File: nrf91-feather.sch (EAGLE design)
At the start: 90 parts, among them J1 CON-USB-1050170001, J2 CON-HEADER-1X12-MALE-PIN, J3 CON-HEADER-1X16-MALE-PIN, J4 CON-1909763-1, J5 CON-SIM-104224-0820, J6 CON-S2B-PH-SM4-TB(LF)(SN), J7 CON-1909763-1, J9 CON-TC2030-MCP-NL, Q1 MOSFET-P-SC89, Q2 MOSFET-DUAL-COMP-SOT563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

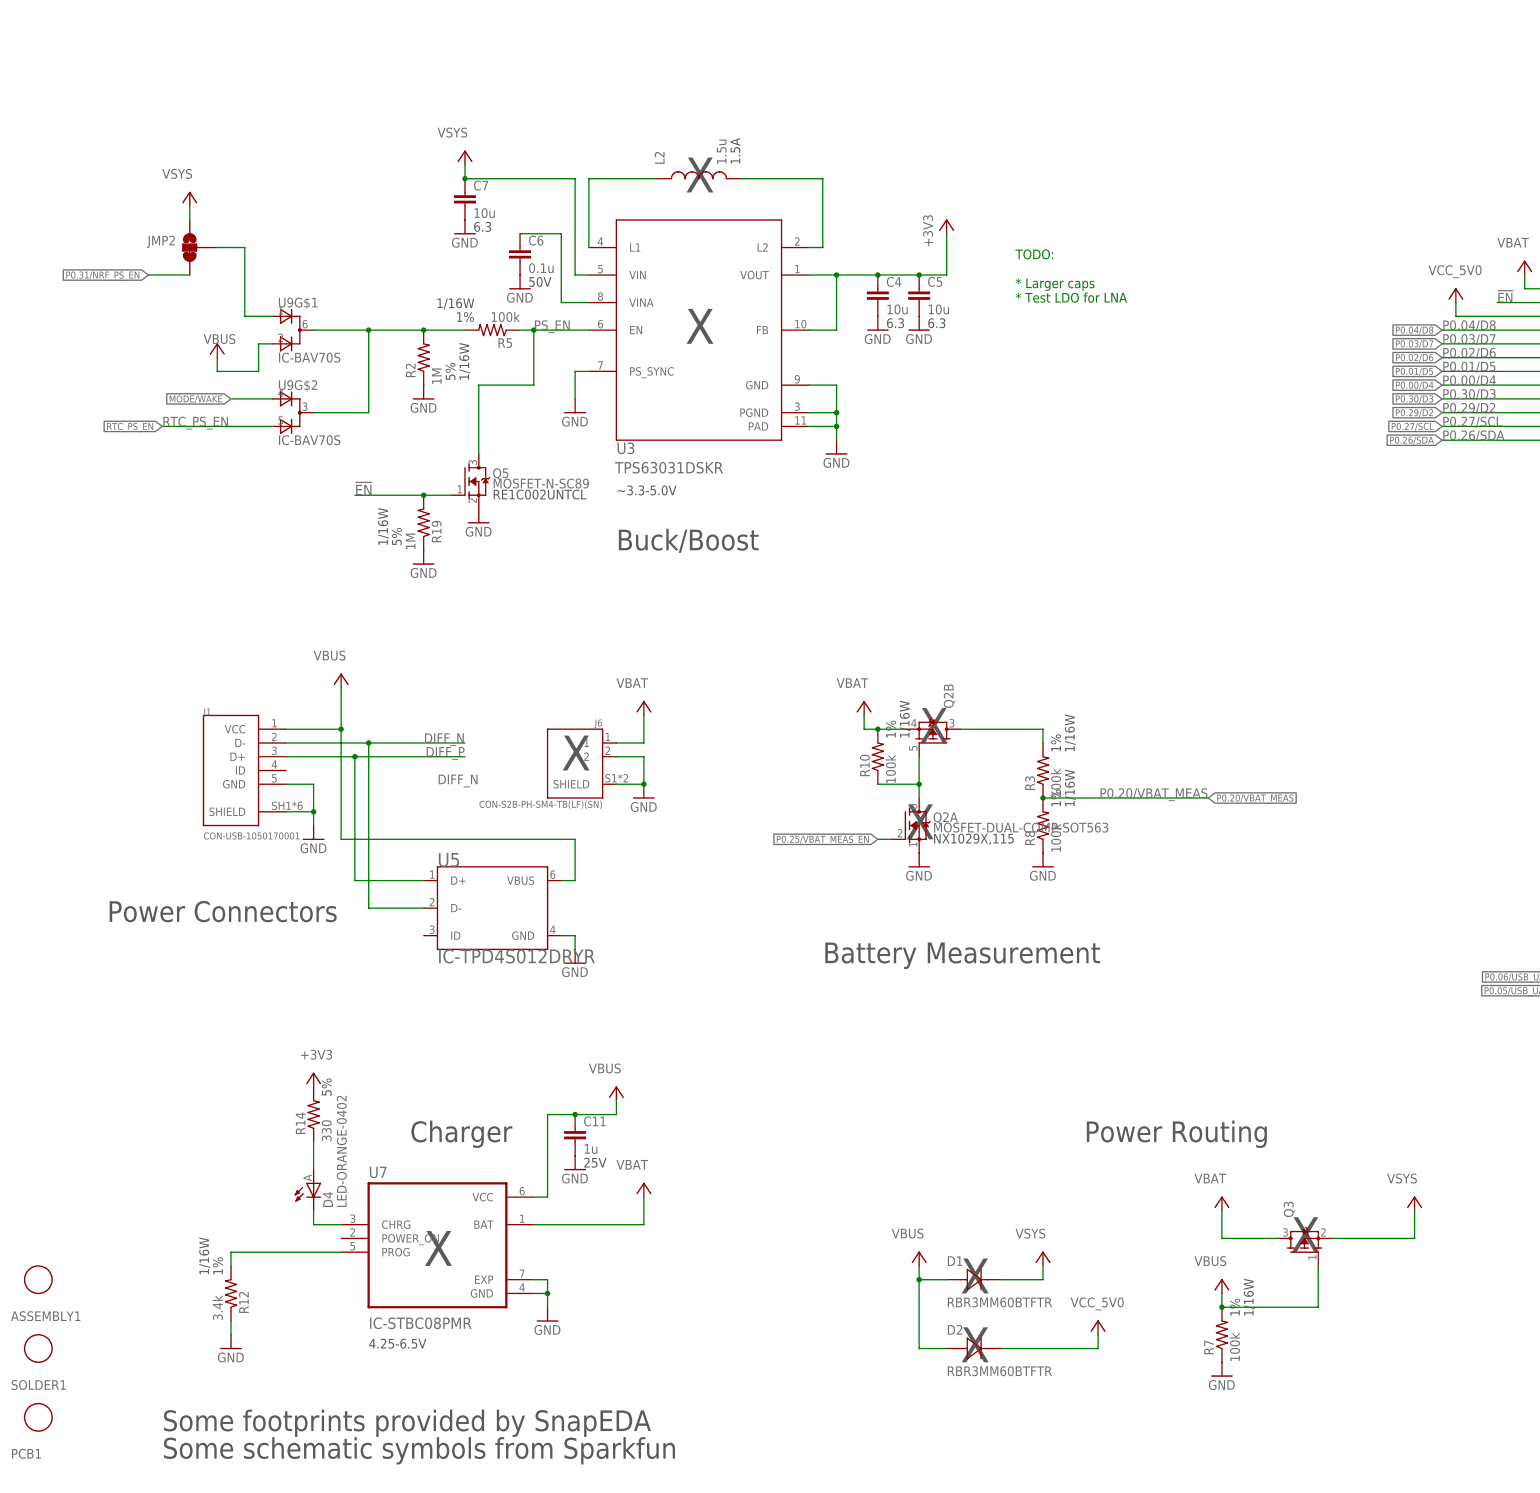
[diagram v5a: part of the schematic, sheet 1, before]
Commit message: Changes for next revision of the nRF9160 Feather
Removed:
* TVS diode

Changed:
* USB is now USB-C
* Power supply is now Boost + LDO combo (not final)
* LED position due to USB-C being larger
* Changed Schottky diodes to a TSC part
* Re-routed and cleaned up some signals on the inner layer
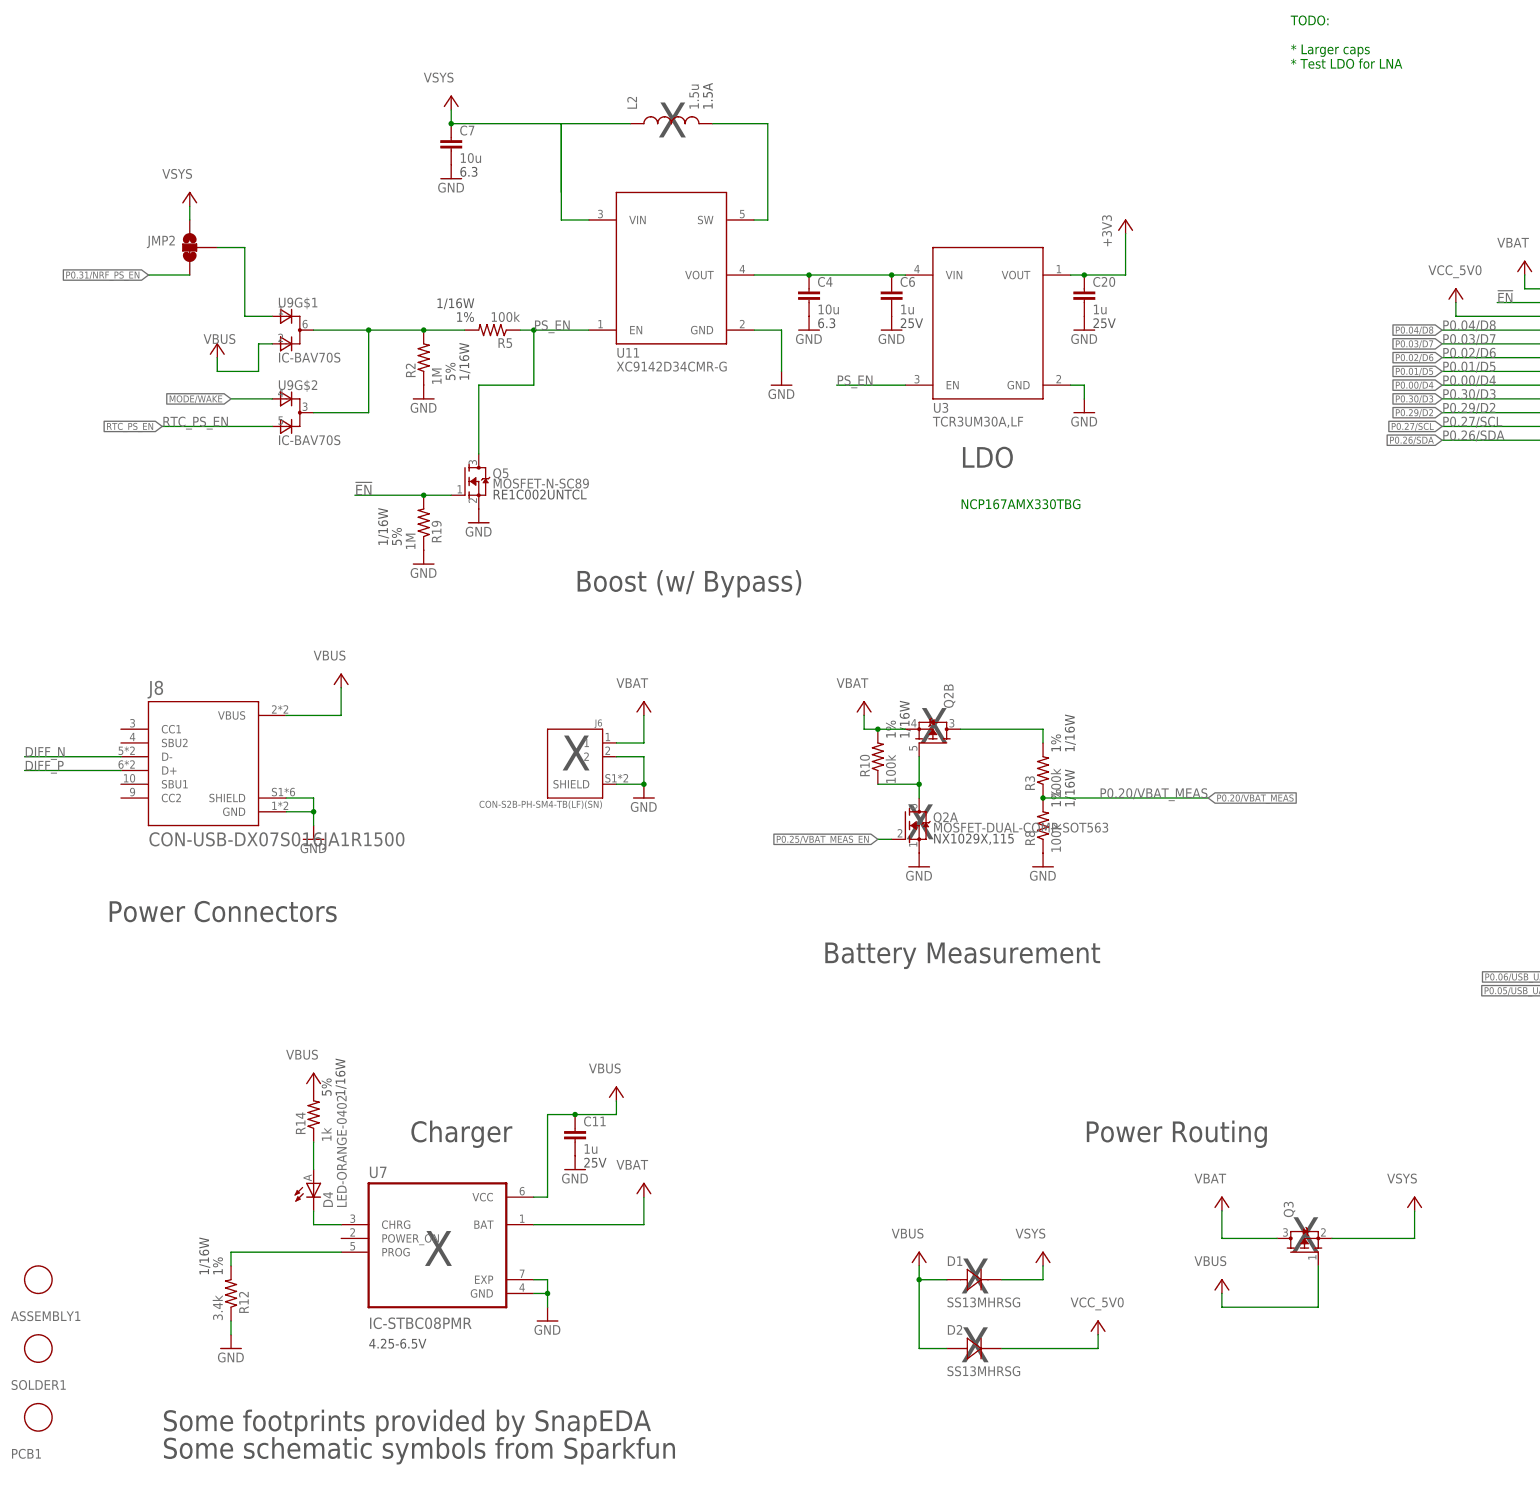
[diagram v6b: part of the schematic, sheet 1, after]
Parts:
- removed C5: 10u, wolff-den:CAP-10U-6.3V-0603
- removed J1: CON-USB-1050170001, wolff-den:CON-USB-1050170001
- removed R7: 100k, wolff-den:RES-100K-1%-0402
- removed U5: IC-TPD4S012DRYR, wolff-den:IC-TPD4S012DRYR
- added C20: 1u, wolff-den:CAP-1U-25V-1-0402
- added J8: CON-USB-DX07S016JA1R1500, wolff-den:CON-USB-DX07S016JA1R1500
- added U11: POWER-VREG-EN-SW-500MA, wolff-den:POWER-VREG-EN-SW-500MA
- C6: value 0.1u -> 1u; device wolff-den:CAP-0.1U-50V-0402 -> wolff-den:CAP-1U-25V-1-0402
- D1, D2: value DIO-SCHOTTKY-3A-01 -> DIO-SCHOTTKY-1A-SMA-MICRO; device wolff-den:DIO-SCHOTTKY-3A-01 -> wolff-den:DIO-SCHOTTKY-1A-SMA-MICRO
- R14: value 330 -> 1k; device wolff-den:RES-330-5%-0402 -> wolff-den:RES-1K-5%-0402
- U3: value IC-TPS63031DSKR -> (none); device wolff-den:IC-TPS63031DSKR -> wolff-den:POWER-VREG-EN-3.0V-DFN4-1X1
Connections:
- removed net N$1: L2.1, U3.L1
- removed net N$14: C6.1, U3.VINA
- new net N$15: C4.1, C6.1, U11.VOUT, U3.VIN
- net +3V3: now also C20.1; no longer C4.1, C5.1, R14.2, U3.FB
- net DIFF_N: now also J8.D-; no longer J1.D-, U5.D-
- net DIFF_P: now also J8.D+; no longer J1.D+, U5.D+
- net GND: now also C20.2, J8.GND, J8.SHIELD, U11.GND; no longer C5.2, J1.GND, J1.SHIELD, R7.1, U3.PAD, U3.PGND, U3.PS_SYNC, U5.GND
- net N$2: now also U11.SW; no longer U3.L2
- net PS_EN: now also U11.EN
- net VBUS: now also J8.VBUS, R14.2; no longer J1.VCC, R7.2, U5.VBUS
- net VSYS: now also L2.1, U11.VIN; no longer U3.VIN
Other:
- note added: "Boost (w/ Bypass)"
- note added: "LDO"
- note added: "NCP167AMX330TBG"
- note removed: "Buck/Boost"
- note removed: "~3.3-5.0V"
- moved on the sheet: C4, C6, C7, L2

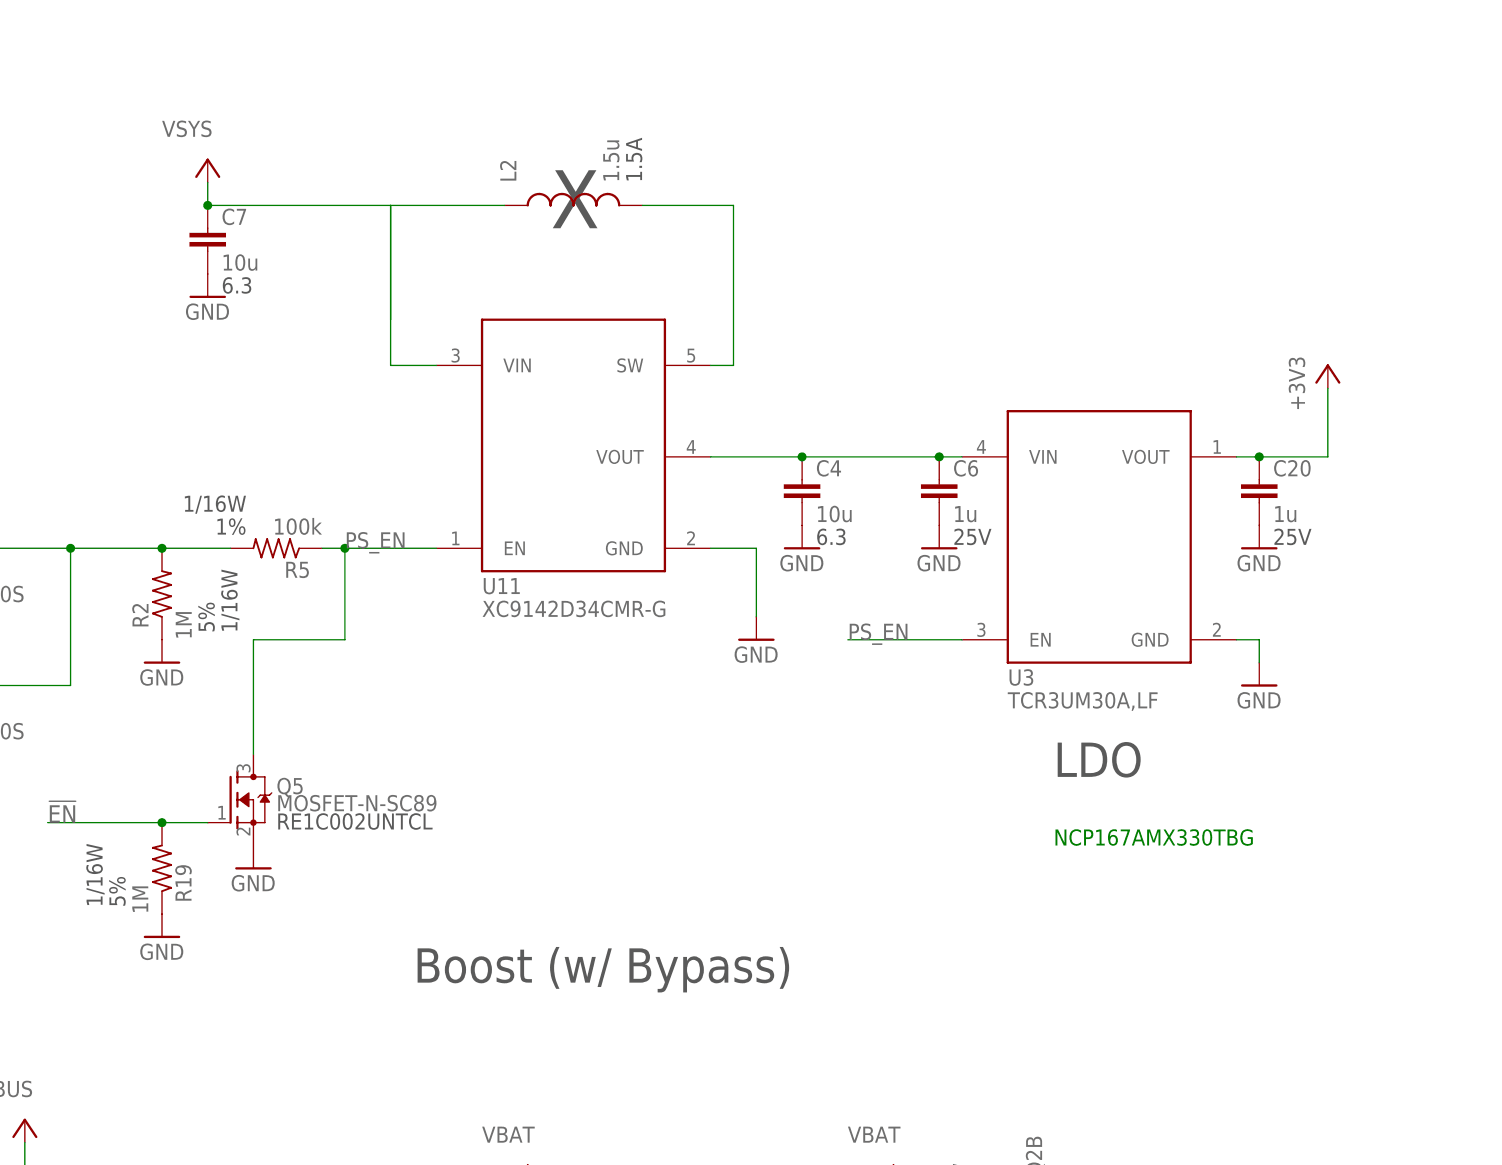
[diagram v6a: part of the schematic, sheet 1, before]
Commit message: Changed up power supply as the Torex part will not work. :(
Changed:
* Power supply to LM3281
* Cleaned up solder mask/paste mask for USB
* Removed paste mask for jumper

Added:
* Connection for enable pin to P0.13
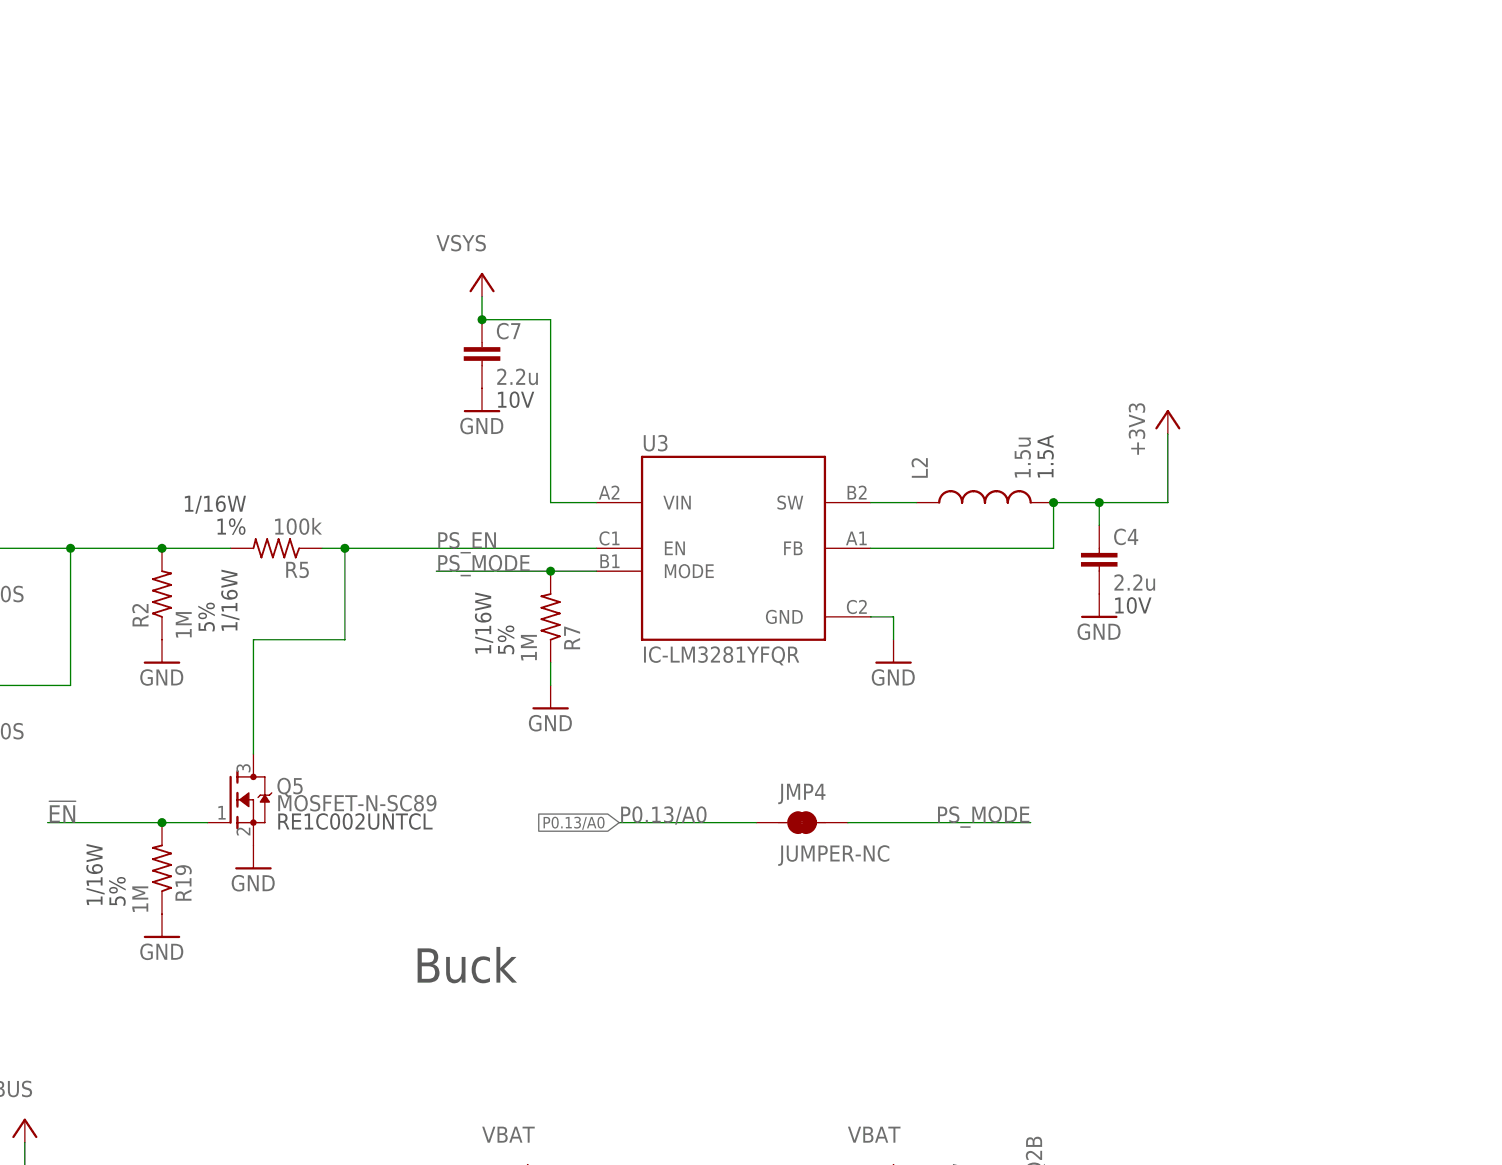
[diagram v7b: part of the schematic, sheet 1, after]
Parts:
- removed C20, C6: 1u, wolff-den:CAP-1U-25V-1-0402
- removed U11: POWER-VREG-EN-SW-500MA, wolff-den:POWER-VREG-EN-SW-500MA
- added JMP4: JUMPER-NC, wolff-den:JUMPER-NC
- added R7: 1M, wolff-den:RES-1M-5%-0402
- C4, C7: value 10u -> 2.2u; device wolff-den:CAP-10U-6.3V-0603 -> wolff-den:CAP-2.2U-10V-01-0603
- U3: value (none) -> IC-LM3281YFQR; device wolff-den:POWER-VREG-EN-3.0V-DFN4-1X1 -> wolff-den:IC-LM3281YFQR
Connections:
- removed net N$15: C4.1, C6.1, U11.VOUT, U3.VIN
- removed net N$2: L2.2, U11.SW
- new net PS_MODE: JMP4.2, R7.2, U3.MODE
- new net PS_SW: L2.1, U3.SW
- net +3V3: now also C4.1, L2.2, U3.FB; no longer C20.1, U3.VOUT
- net GND: now also R7.1; no longer C20.2, C6.2, U11.GND
- net P0.13/A0: now also JMP4.1
- net PS_EN: no longer U11.EN
- net VSYS: now also U3.VIN; no longer L2.1, U11.VIN
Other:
- note added: "Buck"
- note removed: "Boost (w/ Bypass)"
- note removed: "LDO"
- note removed: "NCP167AMX330TBG"
- moved on the sheet: C4, C7, L2
